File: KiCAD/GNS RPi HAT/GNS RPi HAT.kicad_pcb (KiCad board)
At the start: 2 copper layers, 65 x 56.5 mm, 24 parts, among them J1 RPi_GPIO, J3 Conn_01x03_Pin, U2 CAT24C128, U3 PCF8574AT

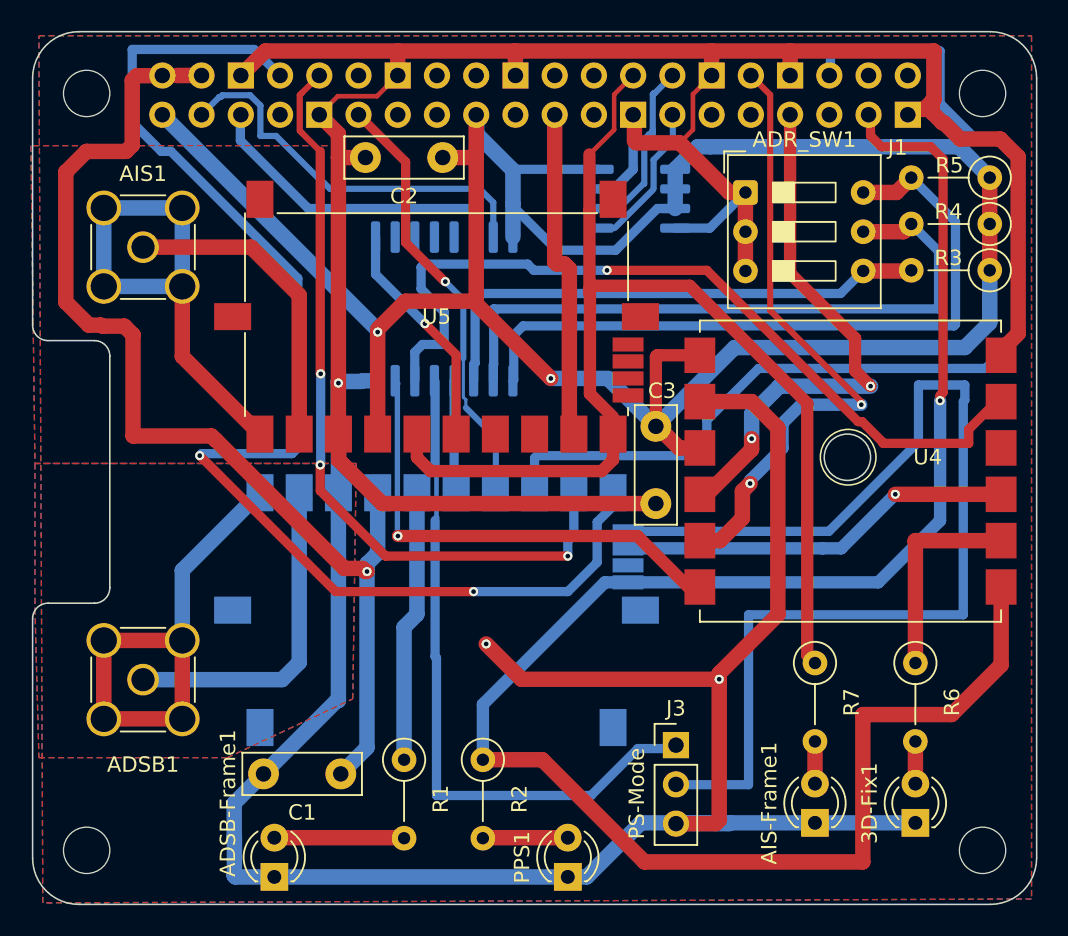
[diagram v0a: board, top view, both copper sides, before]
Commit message: Wechsel auf SMD-Bauteile, Fehlerkorrekturen
Die Widerstände und Leds wurden auf noch von Hand Lötbare SMD-Varianten geändert.
Die Platine wurde weiter aufgeräumt.
Wichtigste Änderung: die Adressierung des I2C Busses für die HAT+ Erkennung wurde von einer fixen Adresse auf Lötpads geändert.
Die Adressen 0x50, 0x51 und ggf. später weitere sind nun möglich um im Abhängigkeit zu anderen HAT keinen Adresskonflikt zu verursachen.
Das erste Design hatte noch fix die Adresse 0x5F, welcher in der Spec nicht automatisch erkannt wird.
Der Schreibschutz ist ebenfalls über eine Lötbrücke steuerbar.
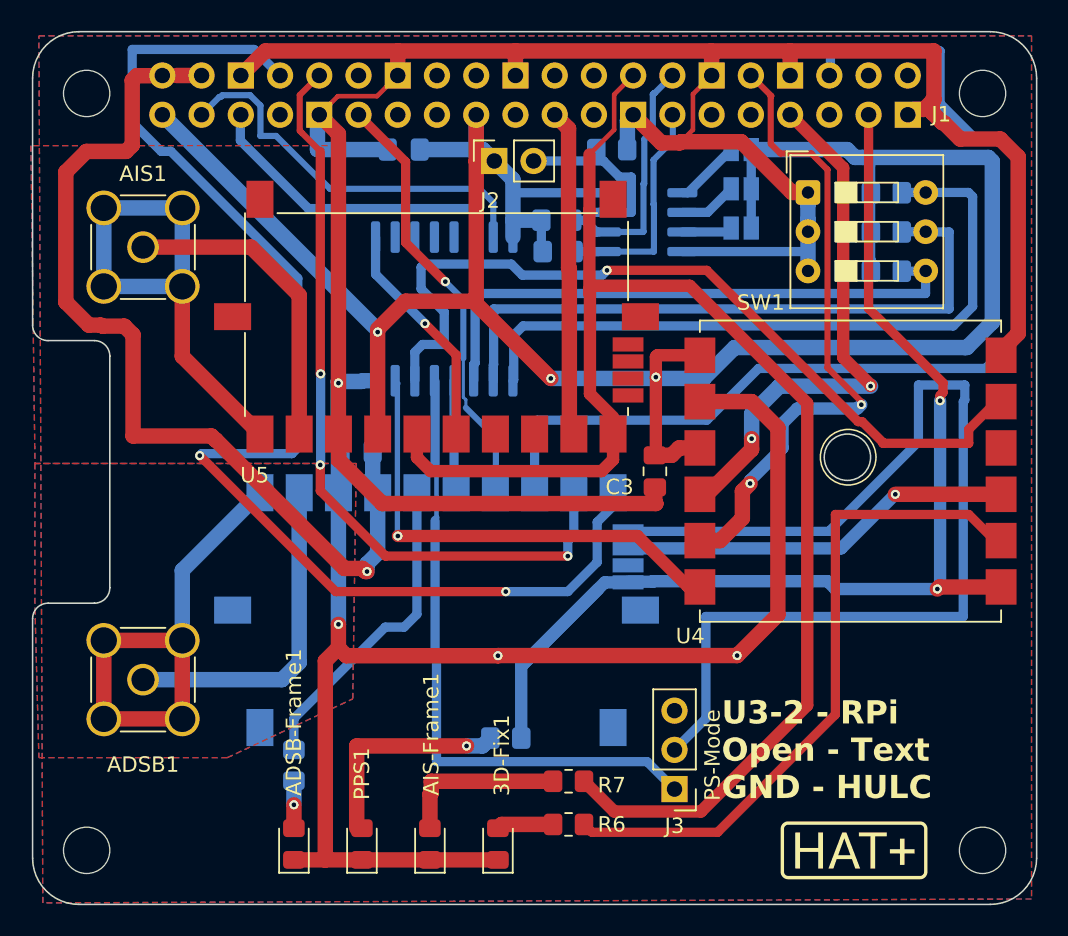
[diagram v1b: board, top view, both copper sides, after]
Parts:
- added A0: Conn_01x02, Jumper:SolderJumper-2_P1.3mm_Open_Pad1.0x1.5mm, B.Cu at (141.2, 75.2)
- added A1: Conn_01x02, Jumper:SolderJumper-2_P1.3mm_Open_Pad1.0x1.5mm, B.Cu at (141.2, 77.7)
- added A2: Conn_01x02, Jumper:SolderJumper-2_P1.3mm_Open_Pad1.0x1.5mm, B.Cu at (141.2, 80.3)
- added J2: Conn_01x02, Connector_PinSocket_2.54mm:PinSocket_1x02_P2.54mm_Vertical, F.Cu at (125.2, 75.9)
- added R10: 3K9, Resistor_SMD:R_0805_2012Metric_Pad1.20x1.40mm_HandSolder, B.Cu at (132.8, 75.2)
- added R8: 3K9, Resistor_SMD:R_0805_2012Metric_Pad1.20x1.40mm_HandSolder, B.Cu at (129.3, 79.8)
- added R9: 3K9, Resistor_SMD:R_0805_2012Metric_Pad1.20x1.40mm_HandSolder, B.Cu at (129.4, 81.8)
- 3D-Fix1, ADSB-Frame1, AIS-Frame1, PPS1: footprint LED_THT:LED_D3.0mm -> LED_SMD:LED_0805_2012Metric_Pad1.15x1.40mm_HandSolder
- C1, C2: footprint Capacitor_THT:C_Disc_D7.5mm_W2.5mm_P5.00mm -> Capacitor_SMD:C_0805_2012Metric_Pad1.18x1.45mm_HandSolder; moved to B.Cu
- C3: footprint Capacitor_THT:C_Disc_D7.5mm_W2.5mm_P5.00mm -> Capacitor_SMD:C_0805_2012Metric_Pad1.18x1.45mm_HandSolder
- R1, R2, R3, R4, R5: footprint Resistor_THT:R_Axial_DIN0207_L6.3mm_D2.5mm_P5.08mm_Vertical -> Resistor_SMD:R_0805_2012Metric_Pad1.20x1.40mm_HandSolder; moved to B.Cu
- R6, R7: footprint Resistor_THT:R_Axial_DIN0207_L6.3mm_D2.5mm_P5.08mm_Vertical -> Resistor_SMD:R_0805_2012Metric_Pad1.20x1.40mm_HandSolder
- moved 3D-Fix1 27.1 mm to (125.5, 120.1)
- moved AIS-Frame1 25.0 mm to (121.1, 120.1)
- moved R6 24.8 mm to (130.0, 118.9), turned to 180 degrees
- moved C1 20.9 mm to (116.3, 94.7)
- moved R7 17.7 mm to (130.0, 116.1), turned to 180 degrees
- moved PPS1 13.5 mm to (116.7, 120.1)
- moved R1 7.14 mm to (112.3, 115.0)
- moved R5 6.76 mm to (150.6, 78.0), turned to 0 degrees
- moved R4 6.71 mm to (150.6, 80.5), turned to 0 degrees
- moved R3 6.69 mm to (150.6, 83.1), turned to 0 degrees
- moved SW1 4.05 mm to (145.5, 78.0)
- moved C3 2.91 mm to (135.6, 96.0)
- moved J3 2.85 mm to (136.9, 116.6), turned to 180 degrees
- moved C2 2.57 mm to (119.4, 75.2)
- moved ADSB-Frame1 2.48 mm to (112.3, 120.1)
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- renumbered ADR_SW1 to SW1
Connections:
- U2 pad 1: +3.3V -> Net-(A0-Pin_1)
- U2 pad 2: +3.3V -> Net-(A1-Pin_1)
- U2 pad 3: +3.3V -> Net-(A2-Pin_1)
- U2 pad 7: GND -> Net-(J2-Pin_2)
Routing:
- net Net-(J1-BCM26): track 120.5 -> 78.2 mm, vias 1 -> 2
- net GND: track 299.8 -> 263.8 mm, vias 3 -> 4
- net Net-(U4-3D-FIX): track 12.8 -> 43.7 mm
- net Net-(J1-BCM7_CE1): track 75.2 -> 95.9 mm
- net +5V: track 72.0 -> 60.7 mm
- net Net-(J2-Pin_2): track 0.00 -> 11.2 mm
- net Net-(PPS1-A): track 5.47 -> 14.2 mm, vias 0 -> 1
- net Net-(AIS-Frame1-A): track 2.47 -> 11.0 mm
- net Net-(ADSB-Frame1-A): track 8.36 -> 3.07 mm, vias 0 -> 1
- net Net-(J1-BCM0_ID_SD): track 9.85 -> 15.0 mm
- net +3.3V: track 162.0 -> 157.3 mm, vias 2 -> 3
- net Net-(J1-BCM1_ID_SC): track 11.5 -> 16.0 mm
- net Net-(A0-Pin_1): track 0.00 -> 4.32 mm
- net Net-(A1-Pin_1): track 0.00 -> 3.79 mm
- net Net-(U3-A2): track 34.5 -> 37.9 mm
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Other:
- board text added: "I2C = 50+x"
- board text added: "U3-2 - RPi Open - Text GND - HULC"
